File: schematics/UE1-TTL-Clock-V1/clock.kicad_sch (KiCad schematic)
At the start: 11 parts, among them U2 74HC4017, U3 NE555, U6 74LS02

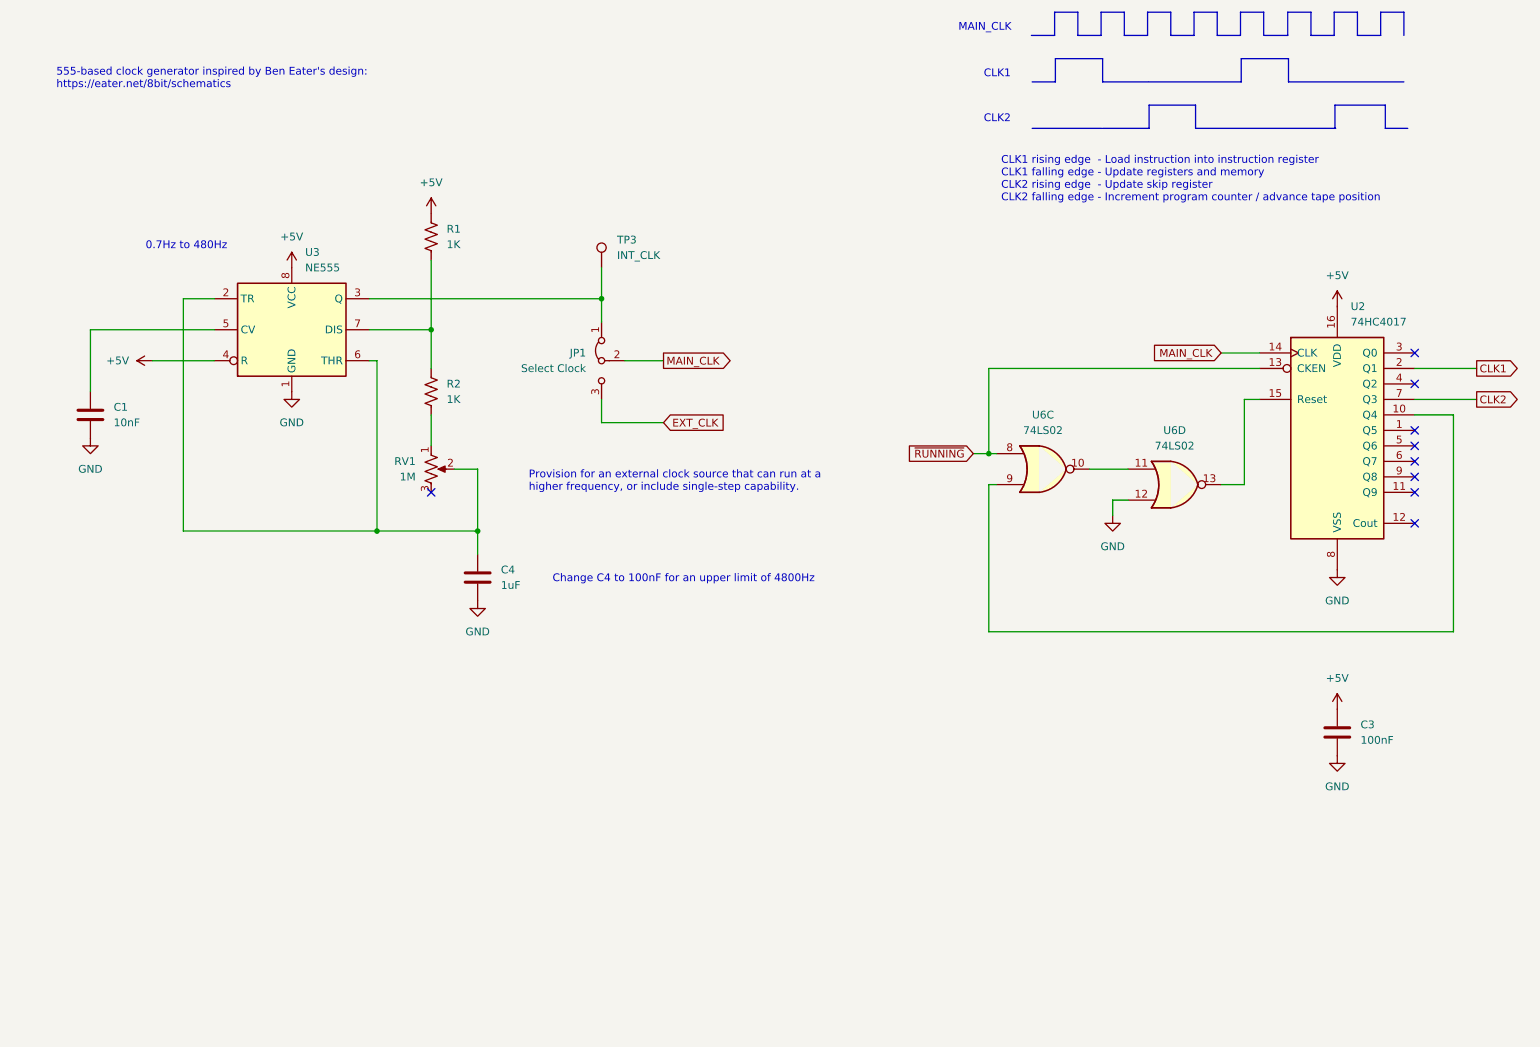
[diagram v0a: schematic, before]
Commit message: Update the clock schematic with V2 modifications
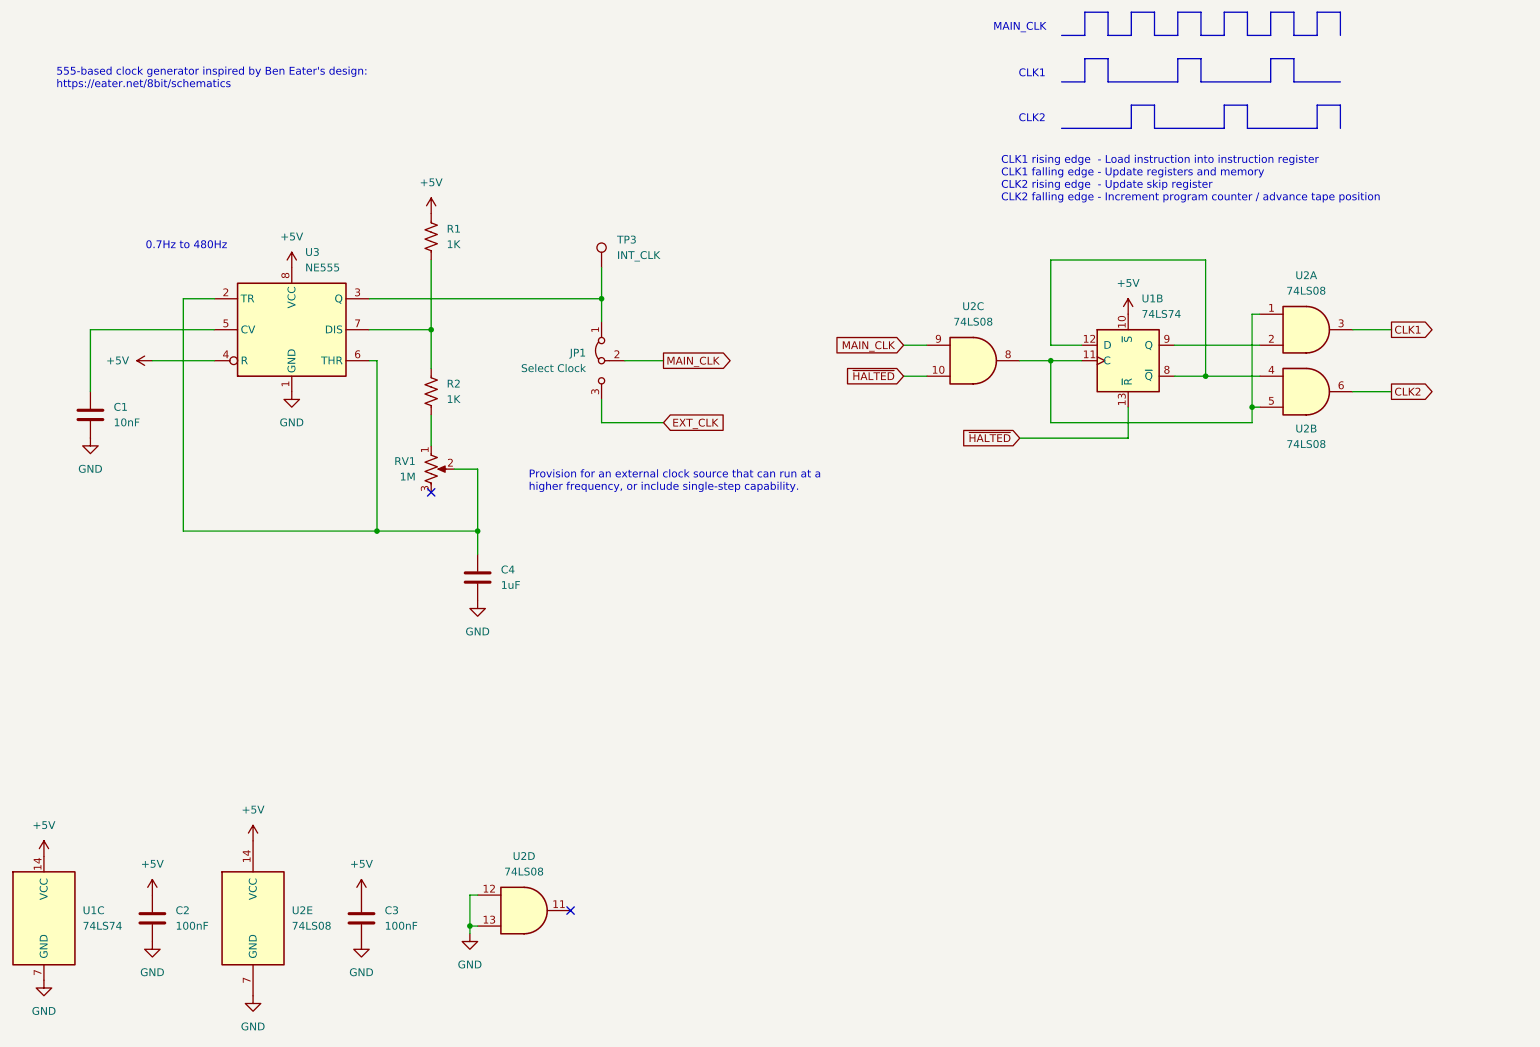
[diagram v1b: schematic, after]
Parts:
- removed U2: 74HC4017, Package_DIP:DIP-16_W7.62mm, symbol 4xxx:4017
- removed U6: 74LS02, Package_DIP:DIP-14_W7.62mm, symbol 74xx:74LS02
- added C2: 100nF, Capacitor_THT:C_Disc_D5.0mm_W2.5mm_P5.00mm, symbol Device:C
- added U1: 74LS74, Package_DIP:DIP-14_W7.62mm, symbol 74xx:74LS74
- added U2: 74LS08, Package_DIP:DIP-14_W7.62mm, symbol 74xx:74LS08
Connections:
- net +5V: now also C2.1, U1.10 (~{S}), U1.14 (VCC), U2.14 (VCC)
- net CLK1: now also U2.3
- net CLK2: now also U2.6
- net GND: now also C2.2, U1.7 (GND), U2.12, U2.13, U2.7 (GND)
- net MAIN_CLK: now also U2.9
- new net: U1.11 (C), U2.1, U2.5, U2.8
- new net: U1.12 (D), U1.8 (~{Q}), U2.4
- new net: U1.9 (Q), U2.2
- new net ~{HALTED}: U1.13 (~{R}), U2.10
- no-connect marks 9 -> 2
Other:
- note removed: "Change C4 to 100nF for an upper limit of 4800Hz"
- moved on the sheet: C3
